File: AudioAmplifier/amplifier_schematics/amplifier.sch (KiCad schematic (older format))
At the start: 1 part

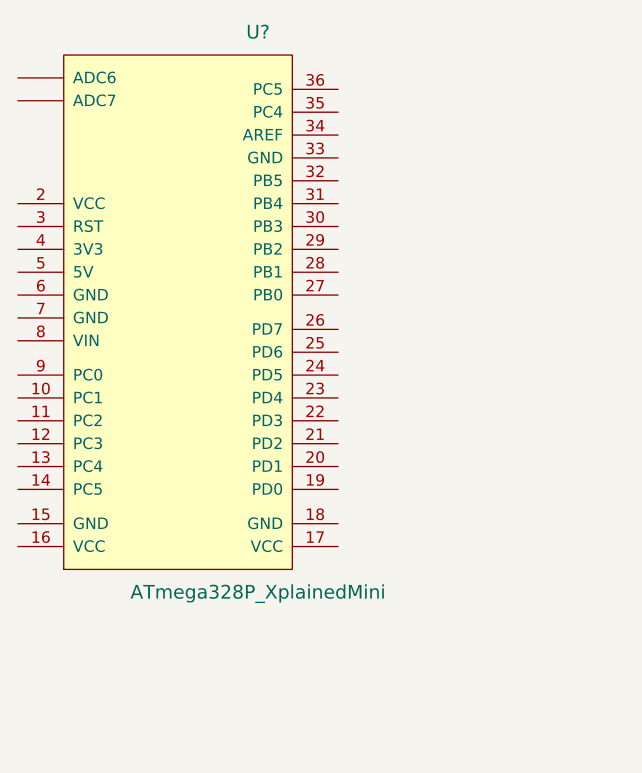
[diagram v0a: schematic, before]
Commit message: updated kicad file and avr menu
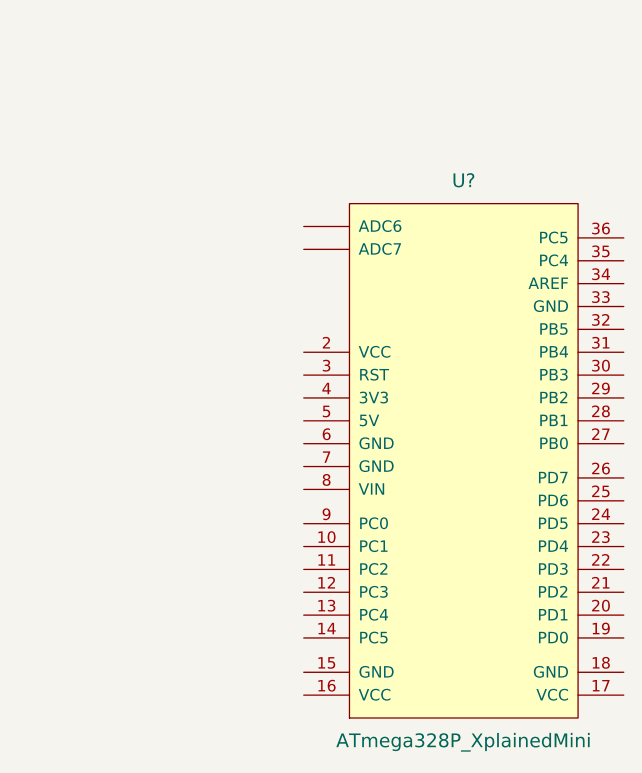
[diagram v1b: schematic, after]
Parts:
- removed U?: ATmega328P_XplainedMini, symbol ATmega328P_XplainedMini
- added U?: ATmega328P_XplainedMini, symbol ATmega328P_XplainedMini
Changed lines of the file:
@@
 $Comp
 L ATmega328P_XplainedMini U?
-U 1 1 58F729DD
-P 3000 4300
-F 0 "U?" H 3000 6550 60  0000 C CNN
-F 1 "ATmega328P_XplainedMini" H 3000 4100 60  0000 C CNN
-F 2 "" H 3000 4300 60  0001 C CNN
-F 3 "" H 3000 4300 60  0001 C CNN
-	1    3000 4300
+U 1 1 58F9BD38
+P 4250 4950
+F 0 "U?" H 3900 7200 60  0000 C CNN
+F 1 "ATmega328P_XplainedMini" H 3900 4750 60  0000 C CNN
+F 2 "" H 4250 4950 60  0001 C CNN
+F 3 "" H 4250 4950 60  0001 C CNN
+	1    4250 4950
 	1    0    0    -1
 $EndComp

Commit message: changed kicad files
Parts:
- added U?: MCP4161-103E/P, DIP254P762X533-8, symbol MCP4161-103E/P
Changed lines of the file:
@@
+	1    0    0    -1
+$EndComp
+$Comp
+L MCP4161-103E/P U?
+U 1 1 58F9C90C
+P 7850 2600
+F 0 "U?" H 8250 2750 50  0000 L CNN
+F 1 "MCP4161-103E/P" H 7950 2100 50  0000 L CNN
+F 2 "DIP254P762X533-8" H 8000 3100 50  0001 L CNN
+F 3 "PDIP-8 Microchip" H 8000 3200 50  0001 L CNN
+F 4 "MCP4161-103E/P" H 8000 2900 50  0001 L CNN "MP"
+F 5 "0.80 USD" H 8150 3450 50  0001 L CNN "Price"
+F 6 "Good" H 8250 3350 50  0001 L CNN "Availability"
+F 7 "Microchip" H 8150 3300 50  0001 L CNN "MF"
+F 8 "Digital Potentiometer 256POS 10kOhm Single Automotive 8-Pin PDIP Tube" H 7450 3000 50  0001 L CNN "Description"
+	1    7850 2600
 	1    0    0    -1
 $EndComp
